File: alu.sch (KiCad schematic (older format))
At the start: 3 parts, among them U16 74HC86, U20 74HC00, U21 74HC32

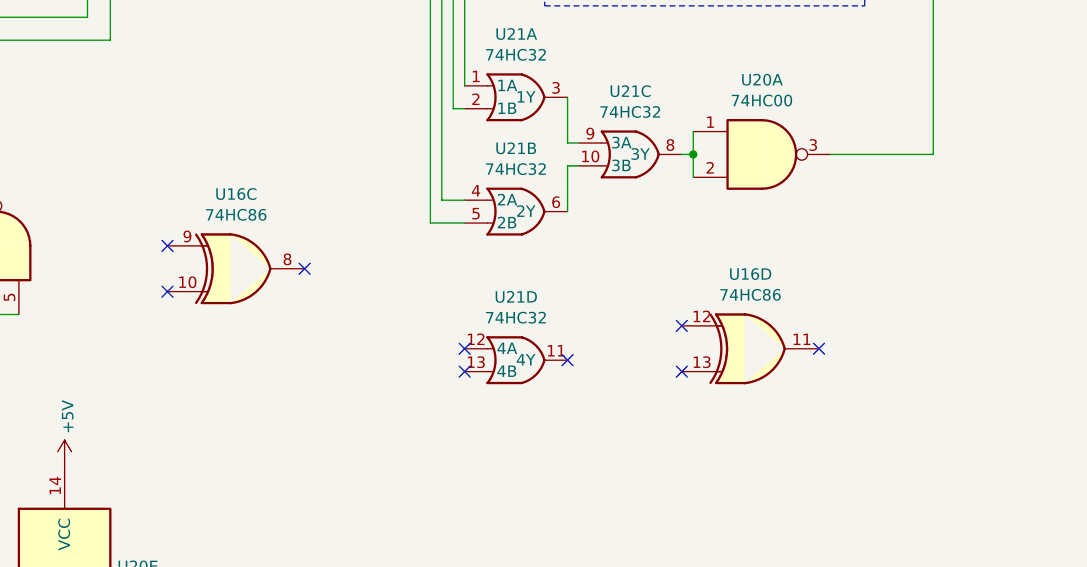
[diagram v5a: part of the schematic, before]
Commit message: fixed some footprints
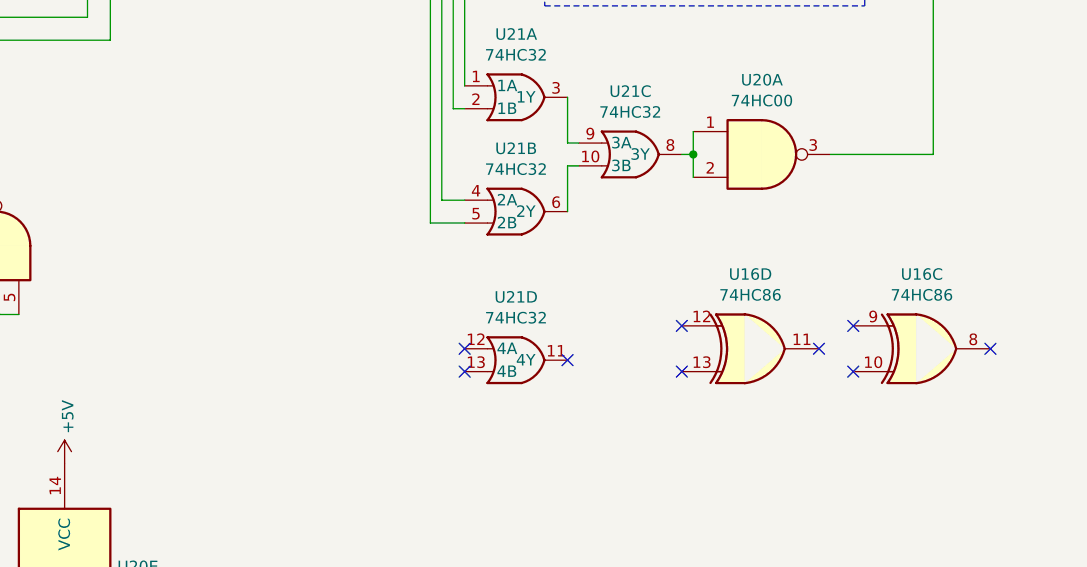
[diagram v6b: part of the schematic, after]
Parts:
- U16: LCSC (none) -> C117522
- U20: footprint (none) -> Package_SO:TSSOP-14_4.4x5mm_P0.65mm
- U20: footprint (none) -> Package_SO:TSSOP-14_4.4x5mm_P0.65mm; LCSC (none) -> C6807
- U21: footprint Housings_SOIC:SOIC-14_3.9x8.7mm_Pitch1.27mm -> Package_SO:SOIC-14_3.9x8.7mm_P1.27mm
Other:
- moved on the sheet: U16C
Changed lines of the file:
@@
 F 0 "U21" H 8325 4975 50  0000 C CNN
 F 1 "74HC32" H 8325 4884 50  0000 C CNN
-F 2 "Housings_SOIC:SOIC-14_3.9x8.7mm_Pitch1.27mm" H 7800 4900 50  0001 C CNN
+F 2 "Package_SO:SOIC-14_3.9x8.7mm_P1.27mm" H 7800 4900 50  0001 C CNN
 F 3 "https://datasheet.lcsc.com/szlcsc/Nexperia-74HC32D-653_C5632.pdf" H 7800 4900 50  0001 C CNN
 F 4 "C5632" H 8350 4700 50  0001 C CNN "LCSC"
@@
 F 0 "U21" H 8825 5225 50  0000 C CNN
 F 1 "74HC32" H 8825 5134 50  0000 C CNN
-F 2 "Housings_SOIC:SOIC-14_3.9x8.7mm_Pitch1.27mm" H 8300 5150 50  0001 C CNN
+F 2 "Package_SO:SOIC-14_3.9x8.7mm_P1.27mm" H 8300 5150 50  0001 C CNN
 F 3 "https://datasheet.lcsc.com/szlcsc/Nexperia-74HC32D-653_C5632.pdf" H 8300 5150 50  0001 C CNN
 F 4 "C5632" H 8850 4950 50  0001 C CNN "LCSC"
@@
 F 0 "U21" H 8325 5475 50  0000 C CNN
 F 1 "74HC32" H 8325 5384 50  0000 C CNN
-F 2 "Housings_SOIC:SOIC-14_3.9x8.7mm_Pitch1.27mm" H 7800 5400 50  0001 C CNN
+F 2 "Package_SO:SOIC-14_3.9x8.7mm_P1.27mm" H 7800 5400 50  0001 C CNN
 F 3 "https://datasheet.lcsc.com/szlcsc/Nexperia-74HC32D-653_C5632.pdf" H 7800 5400 50  0001 C CNN
 F 4 "C5632" H 8350 5200 50  0001 C CNN "LCSC"
@@
 F 0 "U21" H 5725 7425 50  0000 C CNN
 F 1 "74HC32" H 5725 7334 50  0000 C CNN
-F 2 "Housings_SOIC:SOIC-14_3.9x8.7mm_Pitch1.27mm" H 5200 7350 50  0001 C CNN
+F 2 "Package_SO:SOIC-14_3.9x8.7mm_P1.27mm" H 5200 7350 50  0001 C CNN
 F 3 "https://datasheet.lcsc.com/szlcsc/Nexperia-74HC32D-653_C5632.pdf" H 5200 7350 50  0001 C CNN
 F 4 "C5632" H 5750 7150 50  0001 C CNN "LCSC"
@@
 F 0 "U20" H 9400 5275 50  0000 C CNN
 F 1 "74HC00" H 9400 5184 50  0000 C CNN
-F 2 "" H 9400 4950 50  0001 C CNN
+F 2 "Package_SO:TSSOP-14_4.4x5mm_P0.65mm" H 9400 4950 50  0001 C CNN
 F 3 "http://www.ti.com/lit/gpn/sn74hc00" H 9400 4950 50  0001 C CNN
 F 4 "C6807" H 9400 4950 50  0001 C CNN "LCSC"
@@
 F 0 "U20" H 6580 6846 50  0000 L CNN
 F 1 "74HC00" H 6580 6755 50  0000 L CNN
-F 2 "" H 6350 6800 50  0001 C CNN
+F 2 "Package_SO:TSSOP-14_4.4x5mm_P0.65mm" H 6350 6800 50  0001 C CNN
 F 3 "http://www.ti.com/lit/gpn/sn74hc00" H 6350 6800 50  0001 C CNN
 F 4 "C6807" H 6350 6800 50  0001 C CNN "LCSC"
@@
 F 0 "U20" H 6050 5675 50  0000 C CNN
 F 1 "74HC00" H 6050 5584 50  0000 C CNN
-F 2 "" H 6050 5350 50  0001 C CNN
+F 2 "Package_SO:TSSOP-14_4.4x5mm_P0.65mm" H 6050 5350 50  0001 C CNN
 F 3 "http://www.ti.com/lit/gpn/sn74hc00" H 6050 5350 50  0001 C CNN
 F 4 "C6807" H 6050 5350 50  0001 C CNN "LCSC"
@@
 F 0 "U20" V 2696 5170 50  0000 R CNN
 F 1 "74HC00" V 2605 5170 50  0000 R CNN
-F 2 "" H 2650 5350 50  0001 C CNN
+F 2 "Package_SO:TSSOP-14_4.4x5mm_P0.65mm" H 2650 5350 50  0001 C CNN
 F 3 "http://www.ti.com/lit/gpn/sn74hc00" H 2650 5350 50  0001 C CNN
 F 4 "C6807" V 2650 5350 50  0001 C CNN "LCSC"
@@
 F 0 "U20" H 8800 4225 50  0000 C CNN
 F 1 "74HC00" H 8800 4134 50  0000 C CNN
-F 2 "" H 8800 3900 50  0001 C CNN
+F 2 "Package_SO:TSSOP-14_4.4x5mm_P0.65mm" H 8800 3900 50  0001 C CNN
 F 3 "http://www.ti.com/lit/gpn/sn74hc00" H 8800 3900 50  0001 C CNN
+F 4 "C6807" H 8800 3900 50  0001 C CNN "LCSC"
 	4    8800 3900
-	1    0    0    -1
-$EndComp
-$Comp
-L 74xx:74HC86 U16
-U 2 1 6026643A
-P 9400 3800
-F 0 "U16" H 9400 4125 50  0000 C CNN
-F 1 "74HC86" H 9400 4034 50  0000 C CNN
-F 2 "Package_SO:TSSOP-14_4.4x5mm_P0.65mm" H 9400 3800 50  0001 C CNN
-F 3 "https://datasheet.lcsc.com/szlcsc/Texas-Instruments-TI-SN74AHC86PWR_C117522.pdf" H 9400 3800 50  0001 C CNN
-	2    9400 3800
 	1    0    0    -1
 $EndComp
@@
 F 0 "U21" H 8325 6125 50  0000 C CNN
 F 1 "74HC32" H 8325 6034 50  0000 C CNN
-F 2 "Housings_SOIC:SOIC-14_3.9x8.7mm_Pitch1.27mm" H 7800 6050 50  0001 C CNN
+F 2 "Package_SO:SOIC-14_3.9x8.7mm_P1.27mm" H 7800 6050 50  0001 C CNN
 F 3 "https://datasheet.lcsc.com/szlcsc/Nexperia-74HC32D-653_C5632.pdf" H 7800 6050 50  0001 C CNN
 F 4 "C5632" H 8350 5850 50  0001 C CNN "LCSC"
@@
 L 74xx:74HC86 U?
 U 3 1 60302642
-P 7100 5450
+P 10100 5800
 AR Path="/5FEB4D4D/60302642" Ref="U?"  Part="2"
 AR Path="/600A4AF3/600A5215/60302642" Ref="U?"  Part="1"
 AR Path="/600A4AF3/60302642" Ref="U16"  Part="3"
-F 0 "U16" H 7100 5775 50  0000 C CNN
-F 1 "74HC86" H 7100 5684 50  0000 C CNN
-F 2 "Package_SO:TSSOP-14_4.4x5mm_P0.65mm" H 7100 5450 50  0001 C CNN
-F 3 "https://datasheet.lcsc.com/szlcsc/Texas-Instruments-TI-SN74AHC86PWR_C117522.pdf" H 7100 5450 50  0001 C CNN
-F 4 "C117522" H 7100 5450 50  0001 C CNN "LCSC"
-	3    7100 5450
-	1    0    0    -1
-$EndComp
-NoConn ~ 7400 5450
-NoConn ~ 6800 5550
-NoConn ~ 6800 5350
+F 0 "U16" H 10100 6125 50  0000 C CNN
+F 1 "74HC86" H 10100 6034 50  0000 C CNN
+F 2 "Package_SO:TSSOP-14_4.4x5mm_P0.65mm" H 10100 5800 50  0001 C CNN
+F 3 "https://datasheet.lcsc.com/szlcsc/Texas-Instruments-TI-SN74AHC86PWR_C117522.pdf" H 10100 5800 50  0001 C CNN
+F 4 "C117522" H 10100 5800 50  0001 C CNN "LCSC"
+	3    10100 5800
+	1    0    0    -1
+$EndComp
+NoConn ~ 10400 5800
+NoConn ~ 9800 5900
+NoConn ~ 9800 5700
 $Comp
 L 74xx:74HC86 U?
@@
 NoConn ~ 9050 5900
 NoConn ~ 9050 5700
+$Comp
+L 74xx:74HC86 U?
+U 2 1 603622C0
+P 9400 3800
+AR Path="/5FEB4D4D/603622C0" Ref="U?"  Part="2"
+AR Path="/600A4AF3/600A5215/603622C0" Ref="U?"  Part="1"
+AR Path="/600A4AF3/603622C0" Ref="U16"  Part="2"
+F 0 "U16" H 9400 4125 50  0000 C CNN
+F 1 "74HC86" H 9400 4034 50  0000 C CNN
+F 2 "Package_SO:TSSOP-14_4.4x5mm_P0.65mm" H 9400 3800 50  0001 C CNN
+F 3 "https://datasheet.lcsc.com/szlcsc/Texas-Instruments-TI-SN74AHC86PWR_C117522.pdf" H 9400 3800 50  0001 C CNN
+F 4 "C117522" H 9400 3800 50  0001 C CNN "LCSC"
+	2    9400 3800
+	1    0    0    -1
+$EndComp
 $EndSCHEMATC

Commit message: Finished routing
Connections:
- net GND: now also U16.10, U16.12, U16.13, U16.9, U21.12 (4A), U21.13 (4B)
- no-connect marks 9 -> 3
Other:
- moved on the sheet: U16C, U21D
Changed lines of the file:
@@
 Text Notes 8450 3500 0    50   ~ 0
 AND
-$Comp
-L PB170:74HC32 U?
-U 4 1 602AE295
-P 8350 5850
-AR Path="/5FEB4D4D/602AE295" Ref="U?"  Part="1"
-AR Path="/600A4AF3/600A5215/602AE295" Ref="U?"  Part="4"
-AR Path="/600A4AF3/602AE295" Ref="U21"  Part="4"
-F 0 "U21" H 8325 6125 50  0000 C CNN
-F 1 "74HC32" H 8325 6034 50  0000 C CNN
-F 2 "Package_SO:SOIC-14_3.9x8.7mm_P1.27mm" H 7800 6050 50  0001 C CNN
-F 3 "https://datasheet.lcsc.com/szlcsc/Nexperia-74HC32D-653_C5632.pdf" H 7800 6050 50  0001 C CNN
-F 4 "C5632" H 8350 5850 50  0001 C CNN "LCSC"
-	4    8350 5850
-	1    0    0    -1
-$EndComp
-NoConn ~ 8100 5800
-NoConn ~ 8100 5900
-NoConn ~ 8550 5850
+NoConn ~ 8600 5850
 $Comp
 L 74xx:74HC86 U?
 U 3 1 60302642
-P 10100 5800
+P 10200 5850
 AR Path="/5FEB4D4D/60302642" Ref="U?"  Part="2"
 AR Path="/600A4AF3/600A5215/60302642" Ref="U?"  Part="1"
 AR Path="/600A4AF3/60302642" Ref="U16"  Part="3"
-F 0 "U16" H 10100 6125 50  0000 C CNN
-F 1 "74HC86" H 10100 6034 50  0000 C CNN
-F 2 "Package_SO:TSSOP-14_4.4x5mm_P0.65mm" H 10100 5800 50  0001 C CNN
-F 3 "https://datasheet.lcsc.com/szlcsc/Texas-Instruments-TI-SN74AHC86PWR_C117522.pdf" H 10100 5800 50  0001 C CNN
-F 4 "C117522" H 10100 5800 50  0001 C CNN "LCSC"
-	3    10100 5800
+F 0 "U16" H 10200 6175 50  0000 C CNN
+F 1 "74HC86" H 10200 6084 50  0000 C CNN
+F 2 "Package_SO:TSSOP-14_4.4x5mm_P0.65mm" H 10200 5850 50  0001 C CNN
+F 3 "https://datasheet.lcsc.com/szlcsc/Texas-Instruments-TI-SN74AHC86PWR_C117522.pdf" H 10200 5850 50  0001 C CNN
+F 4 "C117522" H 10200 5850 50  0001 C CNN "LCSC"
+	3    10200 5850
 	1    0    0    -1
 $EndComp
-NoConn ~ 10400 5800
-NoConn ~ 9800 5900
-NoConn ~ 9800 5700
+NoConn ~ 10500 5850
 $Comp
 L 74xx:74HC86 U?
@@
 $EndComp
 NoConn ~ 9650 5800
-NoConn ~ 9050 5900
-NoConn ~ 9050 5700
 $Comp
 L 74xx:74HC86 U?
@@
 	1    0    0    -1
 $EndComp
+$Comp
+L PB170:74HC32 U?
+U 4 1 602AE295
+P 8400 5850
+AR Path="/5FEB4D4D/602AE295" Ref="U?"  Part="1"
+AR Path="/600A4AF3/600A5215/602AE295" Ref="U?"  Part="4"
+AR Path="/600A4AF3/602AE295" Ref="U21"  Part="4"
+F 0 "U21" H 8375 6125 50  0000 C CNN
+F 1 "74HC32" H 8375 6034 50  0000 C CNN
+F 2 "Package_SO:SOIC-14_3.9x8.7mm_P1.27mm" H 7850 6050 50  0001 C CNN
+F 3 "https://datasheet.lcsc.com/szlcsc/Nexperia-74HC32D-653_C5632.pdf" H 7850 6050 50  0001 C CNN
+F 4 "C5632" H 8400 5850 50  0001 C CNN "LCSC"
+	4    8400 5850
+	1    0    0    -1
+$EndComp
+$Comp
+L power:GND #PWR?
+U 1 1 602DB418
+P 8150 5900
+AR Path="/602DB418" Ref="#PWR?"  Part="1"
+AR Path="/5FEB4D4D/602DB418" Ref="#PWR?"  Part="1"
+AR Path="/600A4AF3/600A5215/602DB418" Ref="#PWR?"  Part="1"
+AR Path="/600A4AF3/602DB418" Ref="#PWR?"  Part="1"
+F 0 "#PWR?" H 8150 5650 50  0001 C CNN
+F 1 "GND" V 8155 5772 50  0000 R CNN
+F 2 "" H 8150 5900 50  0001 C CNN
+F 3 "" H 8150 5900 50  0001 C CNN
+	1    8150 5900
+	0    1    1    0
+$EndComp
+$Comp
+L power:GND #PWR?
+U 1 1 6033FF71
+P 8150 5800
+AR Path="/6033FF71" Ref="#PWR?"  Part="1"
+AR Path="/5FEB4D4D/6033FF71" Ref="#PWR?"  Part="1"
+AR Path="/600A4AF3/600A5215/6033FF71" Ref="#PWR?"  Part="1"
+AR Path="/600A4AF3/6033FF71" Ref="#PWR?"  Part="1"
+F 0 "#PWR?" H 8150 5550 50  0001 C CNN
+F 1 "GND" V 8155 5672 50  0000 R CNN
+F 2 "" H 8150 5800 50  0001 C CNN
+F 3 "" H 8150 5800 50  0001 C CNN
+	1    8150 5800
+	0    1    1    0
+$EndComp
+$Comp
+L power:GND #PWR?
+U 1 1 603764BA
+P 9050 5700
+AR Path="/603764BA" Ref="#PWR?"  Part="1"
+AR Path="/5FEB4D4D/603764BA" Ref="#PWR?"  Part="1"
+AR Path="/600A4AF3/600A5215/603764BA" Ref="#PWR?"  Part="1"
+AR Path="/600A4AF3/603764BA" Ref="#PWR?"  Part="1"
+F 0 "#PWR?" H 9050 5450 50  0001 C CNN
+F 1 "GND" V 9055 5572 50  0000 R CNN
+F 2 "" H 9050 5700 50  0001 C CNN
+F 3 "" H 9050 5700 50  0001 C CNN
+	1    9050 5700
+	0    1    1    0
+$EndComp
+$Comp
+L power:GND #PWR?
+U 1 1 6037A523
+P 9050 5900
+AR Path="/6037A523" Ref="#PWR?"  Part="1"
+AR Path="/5FEB4D4D/6037A523" Ref="#PWR?"  Part="1"
+AR Path="/600A4AF3/600A5215/6037A523" Ref="#PWR?"  Part="1"
+AR Path="/600A4AF3/6037A523" Ref="#PWR?"  Part="1"
+F 0 "#PWR?" H 9050 5650 50  0001 C CNN
+F 1 "GND" V 9055 5772 50  0000 R CNN
+F 2 "" H 9050 5900 50  0001 C CNN
+F 3 "" H 9050 5900 50  0001 C CNN
+	1    9050 5900
+	0    1    1    0
+$EndComp
+$Comp
+L power:GND #PWR?
+U 1 1 603A832C
+P 9900 5950
+AR Path="/603A832C" Ref="#PWR?"  Part="1"
+AR Path="/5FEB4D4D/603A832C" Ref="#PWR?"  Part="1"
+AR Path="/600A4AF3/600A5215/603A832C" Ref="#PWR?"  Part="1"
+AR Path="/600A4AF3/603A832C" Ref="#PWR?"  Part="1"
+F 0 "#PWR?" H 9900 5700 50  0001 C CNN
+F 1 "GND" V 9905 5822 50  0000 R CNN
+F 2 "" H 9900 5950 50  0001 C CNN
+F 3 "" H 9900 5950 50  0001 C CNN
+	1    9900 5950
+	0    1    1    0
+$EndComp
+$Comp
+L power:GND #PWR?
+U 1 1 603AC342
+P 9900 5750
+AR Path="/603AC342" Ref="#PWR?"  Part="1"
+AR Path="/5FEB4D4D/603AC342" Ref="#PWR?"  Part="1"
+AR Path="/600A4AF3/600A5215/603AC342" Ref="#PWR?"  Part="1"
+AR Path="/600A4AF3/603AC342" Ref="#PWR?"  Part="1"
+F 0 "#PWR?" H 9900 5500 50  0001 C CNN
+F 1 "GND" V 9905 5622 50  0000 R CNN
+F 2 "" H 9900 5750 50  0001 C CNN
+F 3 "" H 9900 5750 50  0001 C CNN
+	1    9900 5750
+	0    1    1    0
+$EndComp
 $EndSCHEMATC
